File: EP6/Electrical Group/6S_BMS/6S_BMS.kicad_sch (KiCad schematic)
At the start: 92 parts, among them IC110 NX2301P,215, IC111 NX2301P,215, IC112 NX2301P,215, IC113 NX2301P,215, IC114 NX2301P,215, IC115 NX2301P,215, IC116 ADG728BRUZ, IC117 ADG728BRUZ, J101 Conn_01x02, J102 Conn_01x02, J103 Conn_01x07, K101 G2RL-2, Q101 2N7002, U2 BQ76930DBT

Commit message: update 6S_BMS schematic draft in EP6
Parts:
- removed C110, C111, C112, C113, C114, C115, C127, C128, C129, C130, C131, C132, C137, C138: 10n, Capacitor_SMD:C_0603_1608Metric, symbol Device:C
- removed C116, C117: 100n, Capacitor_SMD:C_0603_1608Metric, symbol Device:C
- removed D101, D111, D112, D113, D114, D115: RED, LED_SMD:LED_0603_1608Metric, symbol Device:LED
- removed IC110, IC111, IC112, IC113, IC114, IC115: NX2301P,215, Package_TO_SOT_SMD:SOT-23, symbol SamacSys_Parts:NX2301P,215
- removed IC116, IC117: ADG728BRUZ, SamacSys_Parts:SOP65P640X120-16N, symbol SamacSys_Parts:ADG728BRUZ
- removed J101: Conn_01x02, Connector_AMASS:AMASS_XT60-M_1x02_P7.20mm_Vertical, symbol Connector_Generic:Conn_01x02
- removed J102: Conn_01x02, Connector_AMASS:AMASS_XT60-F_1x02_P7.20mm_Vertical, symbol Connector_Generic:Conn_01x02
- removed K101: G2RL-2, Relay_THT:Relay_DPDT_Omron_G2RL-2, symbol Relay:G2RL-2
- removed Q101: 2N7002, Package_TO_SOT_SMD:SOT-23, symbol Transistor_FET:2N7002
- removed R101, R111, R112, R113, R114, R115: 510, Resistor_SMD:R_0603_1608Metric, symbol Device:R
- removed R102, R103: 10k, Resistor_SMD:R_0603_1608Metric, symbol Device:R
- removed R104: 1k, Resistor_SMD:R_0603_1608Metric, symbol Device:R
- removed R125, R126, R127, R128, R129, R130, R140, R141, R142, R143, R144, R145: 130, Resistor_SMD:R_2512_6332Metric, symbol Device:R
- removed R155, R156, R157, R158, R159, R160: 3.3k, Resistor_SMD:R_0603_1608Metric, symbol Device:R
- removed R161, R162, R163, R174, R176, R177, R178, R179, R180, R181: 100, Resistor_SMD:R_0603_1608Metric, symbol Device:R
- removed Z110, Z111, Z112, Z113, Z114, Z115: MMSZ4692T1G, Diode_SMD:D_SOD-123, symbol SamacSys_Parts:MMSZ4692T1G
- added C11: 4u7, symbol Device:C_Small
- added C18, C25, C27, C28: 0u1, symbol Device:C_Small
- added C24: 470p, symbol Device:C_Small
- added C26: 330n, symbol Device:C_Small
- added C29: 1u, symbol Device:C_Small
- added C30, C31, C32, C33: 10u, symbol Device:C_Small
- added D20, D21, D22, D25, D26: diode, symbol Device:D_Small_Filled
- added D24, D6: SS54, symbol Device:D_Shockley
- added D27: 3.6V, symbol Device:D_Zener_Small_Filled
- added F1: main fuse, symbol Device:Fuse_Small
- added J1: BATout, symbol Connector_Generic:Conn_01x02
- added J11: frontBox, symbol Connector_Generic:Conn_01x04
- added J2: GLVMS, symbol Connector_Generic:Conn_01x02
- added J3: switch, symbol Connector_Generic:Conn_01x02
- added J4: BAT EXT, symbol Connector_Generic:Conn_01x02
- added JP2: 3V3 source, symbol Jumper:SolderJumper_3_Open
- added Q10: Q_NMOS-D_Generic_GSD, symbol PCM_Transistor_MOSFET_AKL:Q_NMOS-D_Generic_GSD
- added Q11, Q8: IRLR8726PbF, symbol PCM_Transistor_MOSFET_AKL:Q_NMOS-E_Generic_GDS
- added Q12: AO3401A, PCM_Package_TO_SOT_SMD_AKL:SOT-23, symbol PCM_Transistor_MOSFET_AKL:AO3401A
- added Q7: PMOS, symbol PCM_Transistor_MOSFET_AKL:Q_PMOS-E_Generic_GSD
- added Q9: 2N7002, PCM_Package_TO_SOT_SMD_AKL:SOT-23, symbol PCM_Transistor_MOSFET_AKL:2N7002
- added R40, R41, R42, R49: 100R, symbol Device:R_Small
- added R43: 10R 1%, symbol Device:R_Small
- added R44, R45, R46, R6, R62, R63, R64: 1M, symbol Device:R_Small
- added R47, R48, R54, R55: 10k, symbol Device:R_Small
- added R51: 500k, symbol Device:R_Small
- added R65: 1k, symbol Device:R_Small
- added TP1: REGOUT, symbol Connector:TestPoint_Small
- added U4: 78L05G-AB3-R, PCM_Package_TO_SOT_SMD_AKL:SOT-89-3, symbol PCM_Voltage_Regulator_AKL:L78L05ABU
- added U5: HT7533, Package_TO_SOT_SMD:SOT-89-3, symbol Regulator_Linear:HT75xx-1-SOT89
- J103: value Conn_01x07 -> battery cells
- U2: value BQ76930DBT -> BQ7693003
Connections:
- net VC0 is gone; now on net C0: U2.27 (VC0)
- net VC1 is gone; now on net C1: U2.26 (VC1)
- net VC10 is gone; now on net C6: U2.16 (VC10)
- net VC2 is gone; now on net C2: U2.23 (VC4), U2.24 (VC3), U2.25 (VC2)
- net VC5 is gone; now on net C3: U2.22 (VC5)
- net VC6 is gone; now on net C4: U2.20 (VC6)
- net VC7 is gone; now on net C5: U2.17 (VC9), U2.18 (VC8), U2.19 (VC7)
- net +5V: now also C27.2, C32.2, U4.1 (OUT), U5.2 (VIN)
- net Alert: now also C24.1, R51.1, R6.1
- net C3: now also D20.2 (A)
- net C6: now also D21.2 (A), F1.1, J3.2 (Pin_2), J4.1 (Pin_1), Q10.3 (D), Q12.2 (S), R49.2, R63.1
- net GND: now also U2.3 (VSS), C11.1, C18.1, C24.2, C26.1, C27.1, C28.1, C29.1, C31.1, C32.1, C33.1, D27.2 (A), Q7.1 (G), Q9.2 (S), R41.2, R43.1, R47.2, R55.2, R6.2, R62.2, U4.2, U5.1 (GND); no longer C1.2, H105.1, H106.1, H107.1, H108.1
- net VC5X: now also C1.1, C30.1, C31.2, D20.1 (K), Q10.1 (G), R40.2, R48.2
- net at U2.11 (NC(CAP2)), U2.12 (NC(CAP2)), U2.14 (CAP2): now also C1.2; no longer C1.1
- net DSG: now reaches U2.1 (DSG)
- net DSG: now also Q7.2 (S)
- net TS2: now reaches U2.13 (TS2)
- net TS2: now also R48.1
- net BAT: now reaches U2.15 (BAT)
- net BAT: now also C30.2, D21.1 (K), R49.1
- net CHG: now reaches U2.2 (CHG)
- net CHG: now also Q8.1 (G), R44.1
- net SRP: now reaches U2.28 (SRP)
- net SRP: now also C18.2, C25.1, R41.1
- net SRN: now reaches U2.29 (SRN)
- net SRN: now also C25.2, C28.2, R42.1
- net TS1: now reaches U2.6 (TS1)
- net TS1: now also D25.1 (K), R47.1, R55.1
- net REGSRC: now reaches U2.9 (REGSRC)
- net REGSRC: now also C29.2, Q10.2 (S)
- net Cell0+ renamed CT1
- net Cell1+ renamed CT2
- net Cell2+ renamed CT3
- net CT3: now also R40.1
- net Cell3+ renamed CT4
- net Cell4+ renamed CT5
- net Cell5+ renamed CT6
- net Earth renamed CT0
- net VCC renamed REGOUT
- net REGOUT: now also C11.2, JP2.3 (B), R65.1, TP1.1
- new net: C33.2, JP2.1 (A), U5.3 (VOUT)
- new net: D24.2 (A), Q8.3 (S), R42.2, R43.2, R44.2
- new net: Q12.1 (G), R63.2, R64.1
- new net: F1.2, J2.2 (Pin_2)
- new net: D22.2 (A), Q7.3 (D), R46.1
- new net: D22.1 (K), Q11.1 (G), R45.1, R46.2
- new net: D24.1 (K), D6.1 (K), Q11.2 (D), Q8.2 (D)
- new net: C26.2, Q12.3 (D), U4.3 (IN)
- new net: D26.1 (K), R54.2
- new net: D26.2 (A), J3.1 (Pin_1)
- new net: D25.2 (A), D27.1 (K), R54.1
- new net: Q9.1 (G), R62.1, R65.2
- new net: Q9.3 (D), R64.2
- new net +24V: J1.2 (Pin_2), J11.4 (Pin_4), J2.1 (Pin_1)
- new net +3V3: JP2.2 (C)
- new net MCU/ALERT: R51.2
- new net MCU/CANH: J11.1 (Pin_1)
- new net MCU/CANL: J11.2 (Pin_2)
- new net PACK-: D6.2 (A), H105.1, H106.1, H107.1, H108.1, J1.1 (Pin_1), J11.3 (Pin_3), J4.2 (Pin_2), Q11.3 (S), R45.2
- no-connect marks 2 -> 0
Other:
- added sheet balancing (balancing.kicad_sch)
- sheet MCU ports: added ALERT, CANH, CANL, SCL, SDA, S[1..6], shipTrig; removed none
- note added: "Cf = 10uF"
- note added: "Rf = 100R"
- note added: "Rsns < OCD max / OCD ampere = 100mV / 5A = 20 mohms"
- note added: "alternative SK10x"
- note added: "out connectors: M15 GLVMS M15 BATout M15 BAText M8 4p frontBox (CAN + 24V) button on case battery on display 7seg (voltage + amps)"
- note added: "the only one on jlc that is 3.3 REG out and available"
- note removed: "100V"
- moved on the sheet: C1, C2, F110, F111, F112, F113, F114, F115, F116, H105, H106, H107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

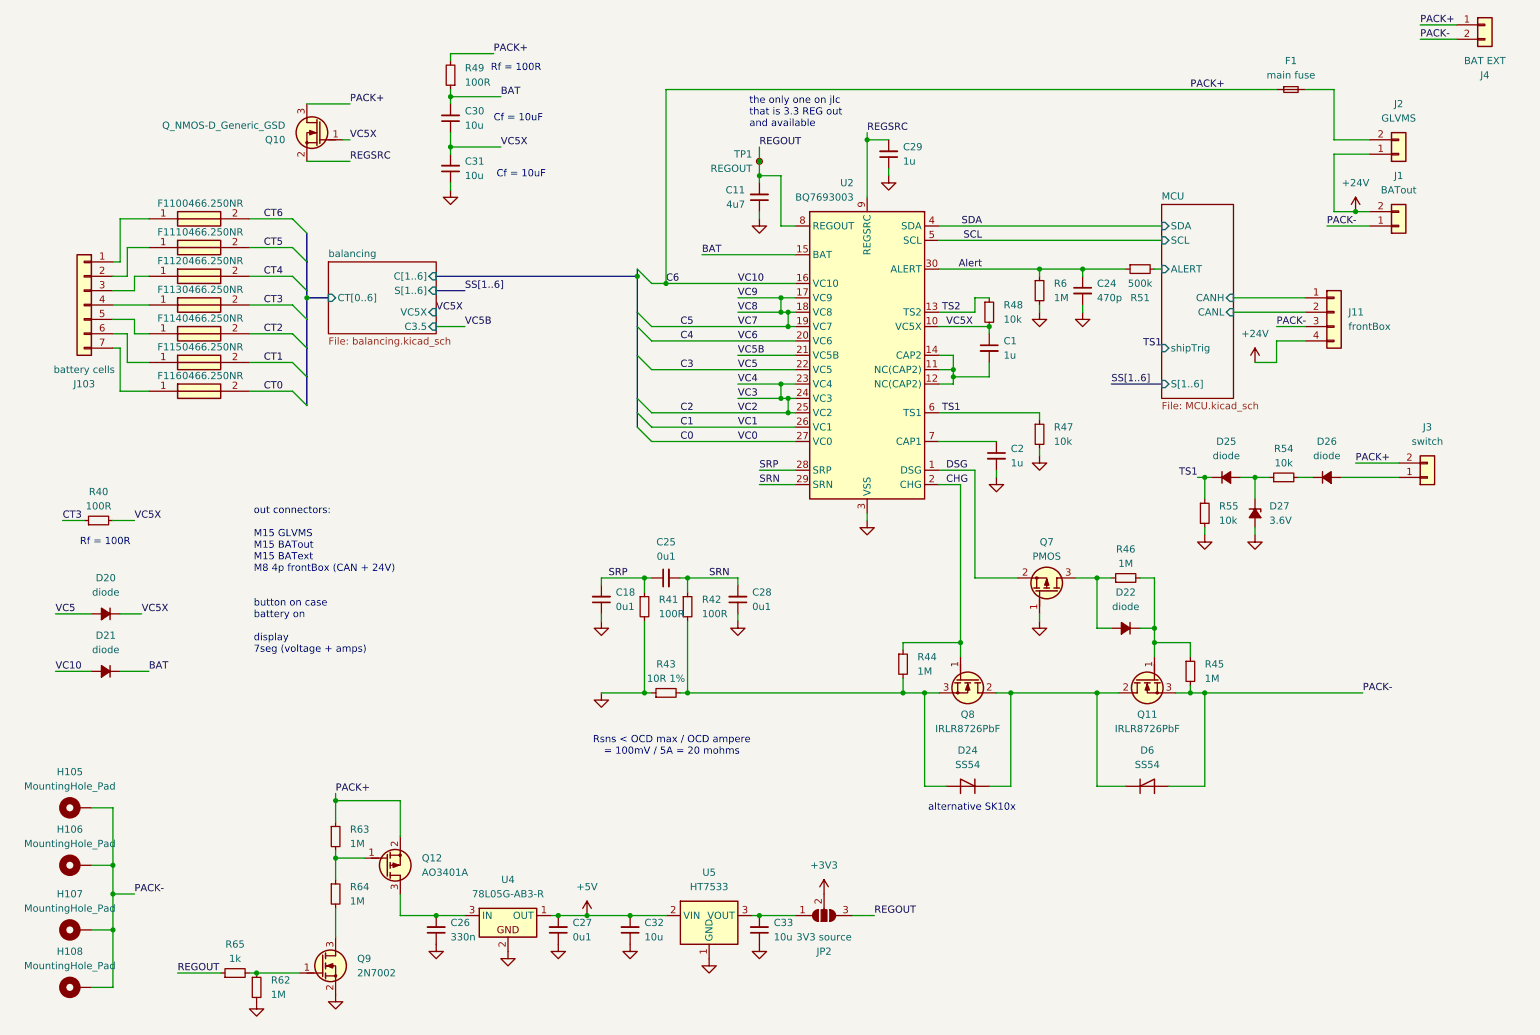
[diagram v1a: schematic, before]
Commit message: update 6S_BMS schematic, for FET and Balancing
use highside FET for charge and discharge switch
and use chip for balance rather than MCU
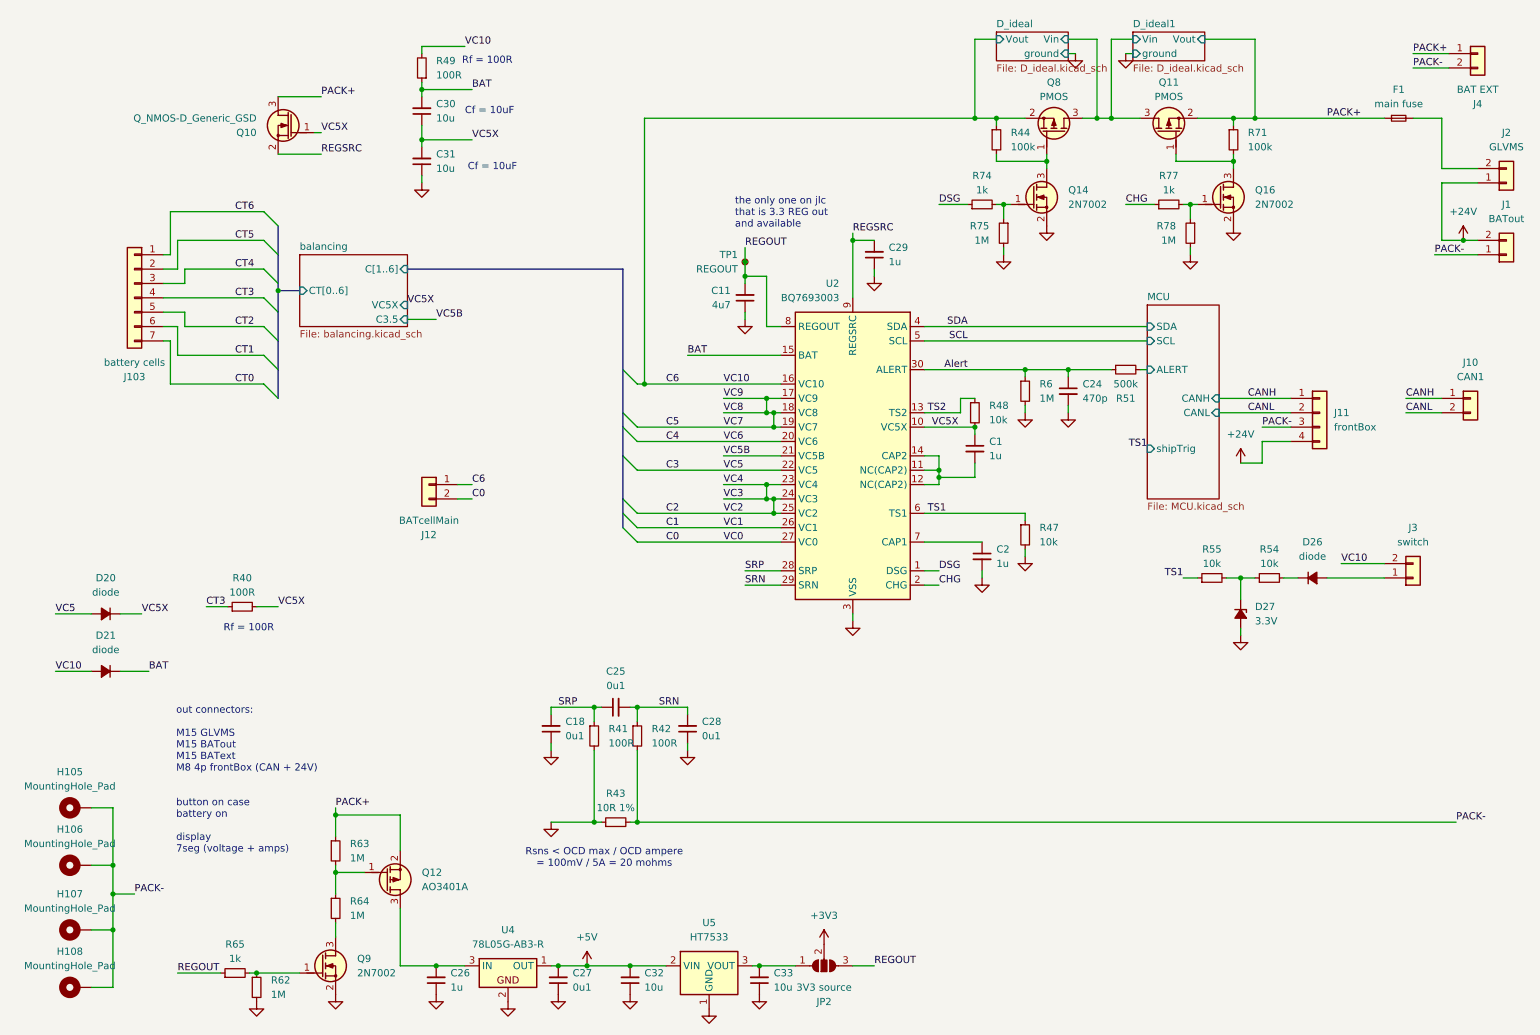
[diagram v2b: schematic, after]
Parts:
- removed D22, D25: diode, symbol Device:D_Small_Filled
- removed D24, D6: SS54, symbol Device:D_Shockley
- removed F110, F111, F112, F113, F114, F115, F116: 0466.250NR, Fuse:Fuse_1206_3216Metric, symbol SamacSys_Parts:0466.250NR
- removed Q11, Q8: IRLR8726PbF, symbol PCM_Transistor_MOSFET_AKL:Q_NMOS-E_Generic_GDS
- removed Q7: PMOS, symbol PCM_Transistor_MOSFET_AKL:Q_PMOS-E_Generic_GSD
- removed R45, R46: 1M, symbol Device:R_Small
- added J10: CAN1, Connector_JST:JST_XH_B2B-XH-A_1x02_P2.50mm_Vertical, symbol Connector_Generic:Conn_01x02
- added J12: BATcellMain, symbol Connector_Generic:Conn_01x02
- added Q11, Q8: PMOS, symbol PCM_Transistor_MOSFET_AKL:Q_PMOS-E_Generic_GSD
- added Q14, Q16: 2N7002, PCM_Package_TO_SOT_SMD_AKL:SOT-23, symbol PCM_Transistor_MOSFET_AKL:2N7002
- added R71: 100k, symbol Device:R_Small
- added R74, R77: 1k, symbol Device:R_Small
- added R75, R78: 1M, symbol Device:R_Small
- C26: value 330n -> 1u
- D27: value 3.6V -> 3.3V
- R44: value 1M -> 100k
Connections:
- net C0: now also J12.2 (Pin_2)
- net C6: now also R44.1, J12.1 (Pin_1), Q8.2 (S); no longer F1.1, J4.1 (Pin_1), Q10.3 (D), Q12.2 (S), R63.1
- net CHG: now also R77.1; no longer R44.1
- net CT0: now also J103.7 (Pin_7)
- net CT1: now also J103.6 (Pin_6)
- net CT2: now also J103.5 (Pin_5)
- net CT3: now also J103.4 (Pin_4)
- net CT4: now also J103.3 (Pin_3)
- net CT5: now also J103.2 (Pin_2)
- net CT6: now also J103.1 (Pin_1)
- net DSG: now also R74.1
- net GND: now also Q14.2 (S), Q16.2 (S), R75.2, R78.2; no longer R55.2
- net PACK-: now also R42.2, R43.2
- net at D27.1 (K), R54.1: now also R55.2
- net MCU/CANH renamed CANH
- net CANH: now also J10.1 (Pin_1)
- net MCU/CANL renamed CANL
- net CANL: now also J10.2 (Pin_2)
- new net: Q11.1 (G), Q16.3 (D), R71.2
- new net: Q16.1 (G), R77.2, R78.1
- new net: Q14.1 (G), R74.2, R75.1
- new net: Q14.3 (D), Q8.1 (G), R44.2
- new net D_ideal/Vin: Q11.3 (D), Q8.3 (D)
- new net PACK+: F1.1, J4.1 (Pin_1), Q10.3 (D), Q11.2 (S), Q12.2 (S), R63.1, R71.1
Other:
- added sheet D_ideal (D_ideal.kicad_sch)
- added sheet D_ideal1 (D_ideal.kicad_sch)
- sheet MCU ports: added none; removed S[1..6]
- sheet balancing ports: added none; removed S[1..6]
- note removed: "alternative SK10x"
- moved on the sheet: C1, C11, C18, C2, C24, C25, C26, C27, C28, C29, C30, C31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
